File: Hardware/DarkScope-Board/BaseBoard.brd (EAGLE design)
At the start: 108 x 87.6 mm, 90 parts, among them IC1 7805DT, IC2 REG1117, IC3 7905, J1 DCJ0202, Q1 8MHz, T2 9014, U1 STM32F103CBT6, X1 TSW-102-07-G-S, X2 TSW-102-07-G-S, X3 MINI-USB-32005-301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

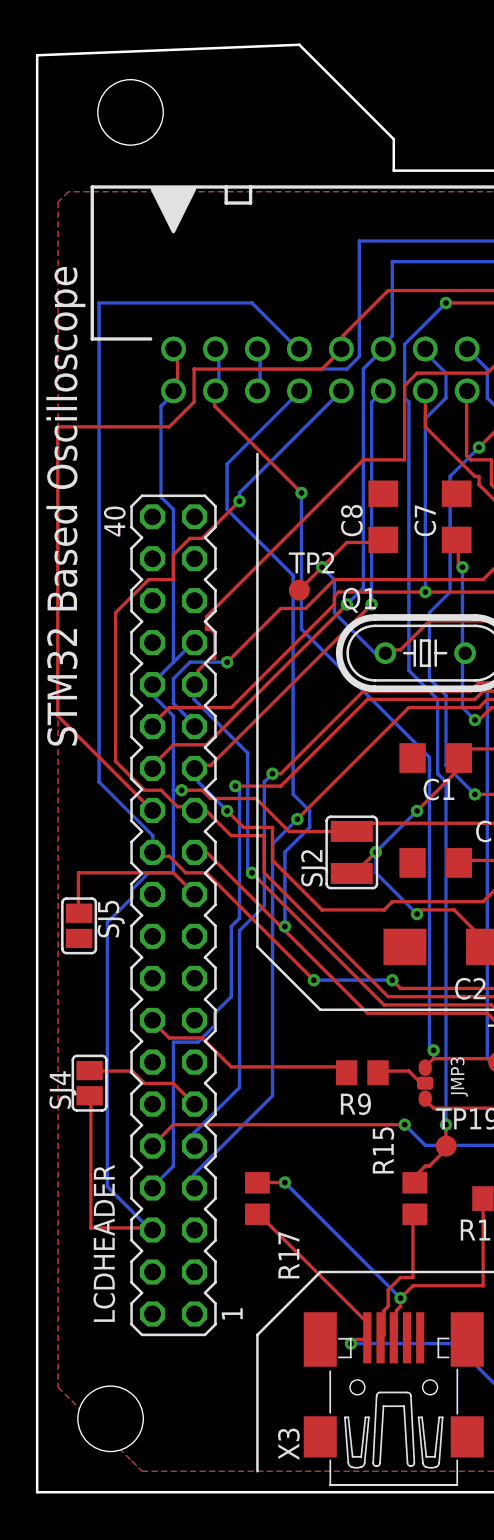
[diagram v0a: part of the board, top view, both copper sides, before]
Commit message: Updated Board Dimension and Added Gerbers
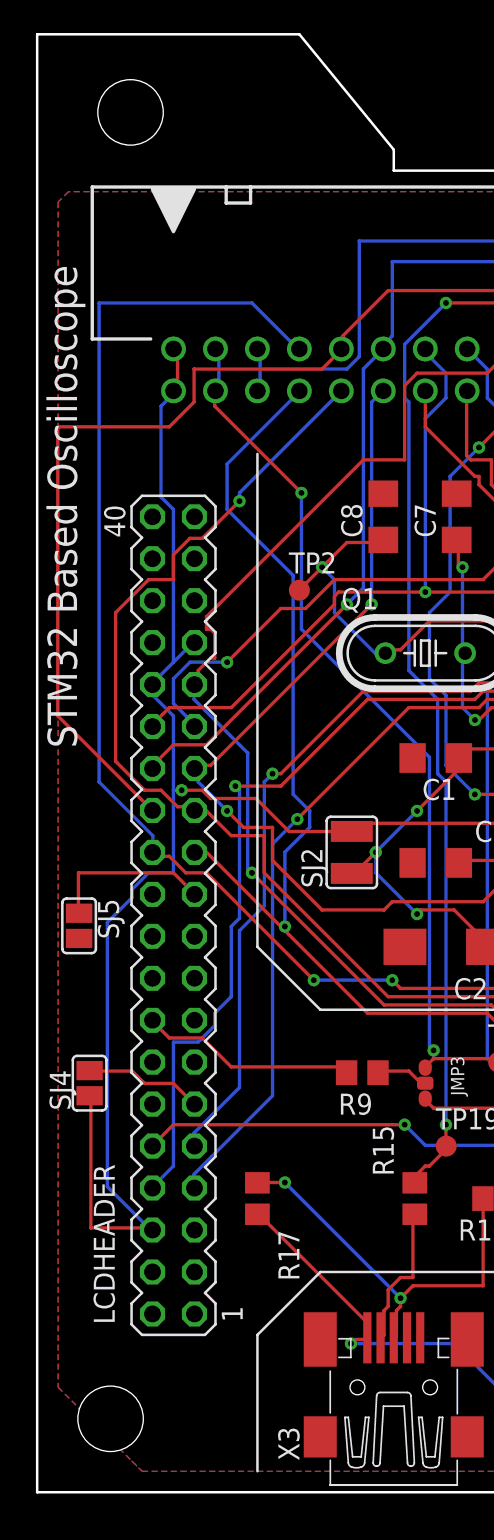
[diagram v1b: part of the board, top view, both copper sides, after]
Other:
- board size 108 x 87.6 mm -> 108 x 88.3 mm
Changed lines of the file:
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@@
 <drawing>
 <settings>
-<setting alwaysvectorfont="no"/>
+<setting alwaysvectorfont="yes"/>
 <setting verticaltext="up"/>
 </settings>
@@
 <wire x1="64.77" y1="3.81" x2="64.77" y2="1.27" width="0.1524" layer="25"/>
 <text x="77.47" y="76.835" size="1.778" layer="25">9V Max</text>
-<wire x1="0" y1="0" x2="0" y2="86.995" width="0.1524" layer="20"/>
-<wire x1="0" y1="86.995" x2="15.875" y2="87.63" width="0.1524" layer="20"/>
-<wire x1="15.875" y1="87.63" x2="21.59" y2="81.915" width="0.1524" layer="20"/>
-<wire x1="21.59" y1="81.915" x2="21.59" y2="80.01" width="0.1524" layer="20"/>
+<wire x1="0" y1="0" x2="0" y2="88.265" width="0.1524" layer="20"/>
+<wire x1="0" y1="88.265" x2="15.875" y2="88.265" width="0.1524" layer="20"/>
+<wire x1="15.875" y1="88.265" x2="21.59" y2="81.28" width="0.1524" layer="20"/>
+<wire x1="21.59" y1="81.28" x2="21.59" y2="80.01" width="0.1524" layer="20"/>
 <wire x1="21.59" y1="80.01" x2="78.74" y2="80.01" width="0.1524" layer="20"/>
 <wire x1="78.74" y1="80.01" x2="78.74" y2="82.55" width="0.1524" layer="20"/>

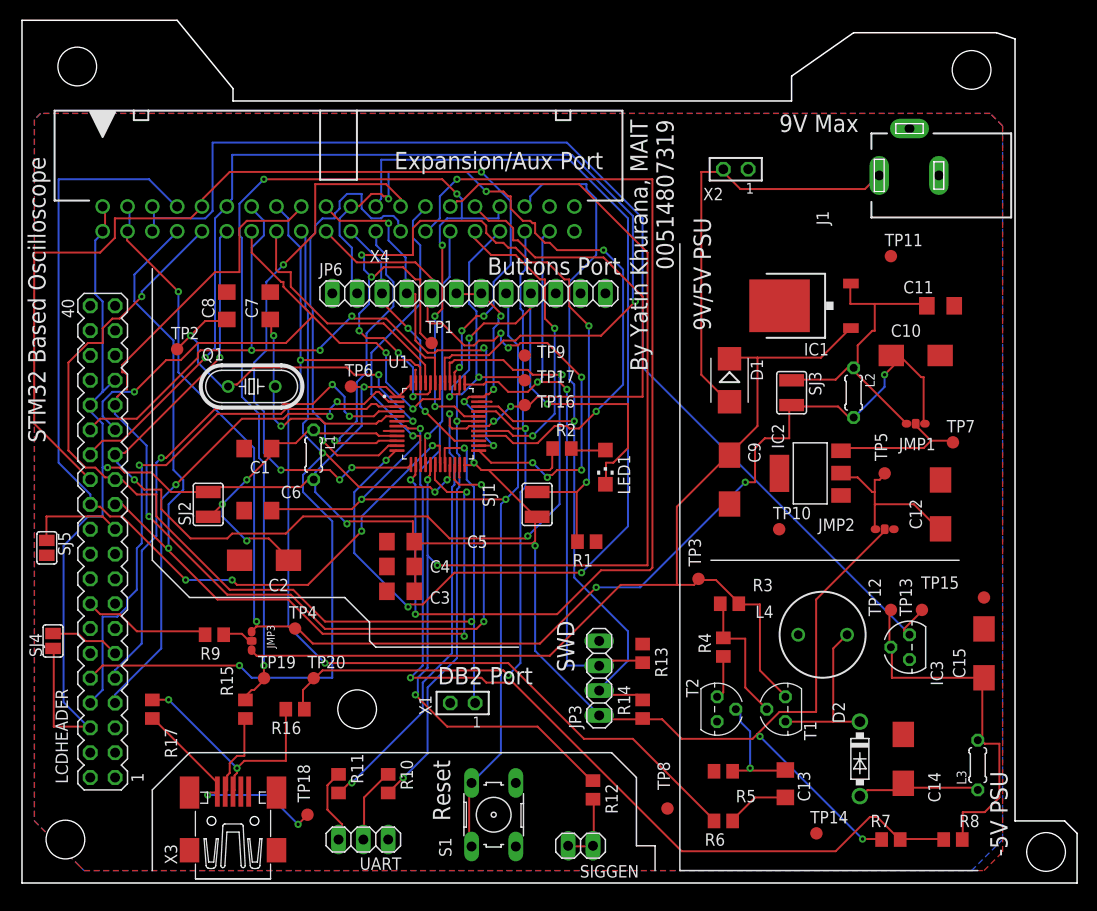
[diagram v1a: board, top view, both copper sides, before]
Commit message: Fixed BaseBoard Bugs
1. Ground Plane Not connected Properly
2. C14,C15 Reversed.
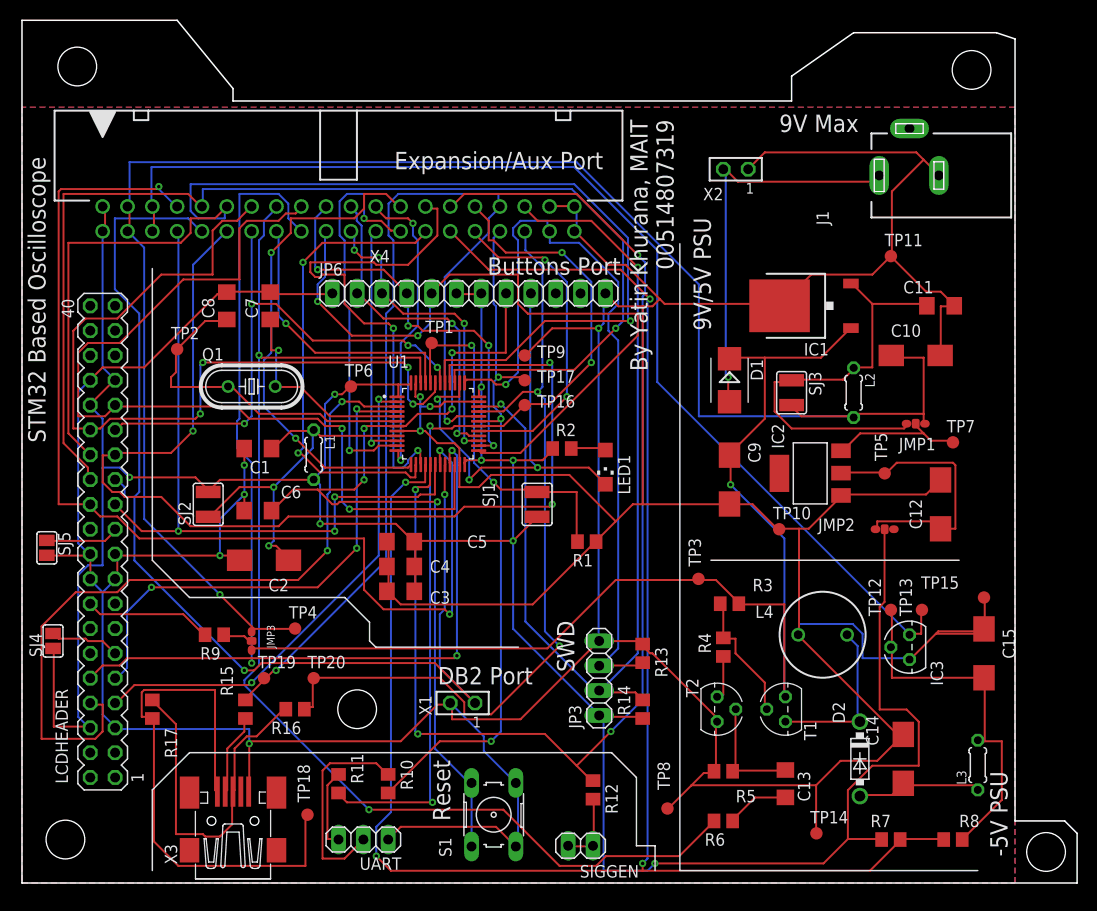
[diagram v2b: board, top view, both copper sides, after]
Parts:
- T1: value (none) -> 8550
- turned C14 to 270 degrees
- turned C15 to 270 degrees
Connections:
- net GND: now also C14.+, C15.+; no longer C14.-, C15.-
- net N$12: now also C14.-; no longer C14.+
- net N$13: now also C15.-; no longer C15.+
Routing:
- net GND: track 5.47 -> 584.9 mm, vias 0 -> 8
- net VSENSEL1: track 110.3 -> 31.2 mm, vias 3 -> 2
- net V-MON: track 116.8 -> 185.5 mm, vias 2 -> 4
- net ADCIN2: track 108.4 -> 48.0 mm, vias 3 -> 2
- net N$21: track 94.1 -> 37.4 mm, vias 7 -> 2
- net BTN1: track 76.4 -> 34.5 mm, vias 4 -> 2
- net N$26: track 23.3 -> 56.4 mm, vias 2 -> 0
- net +5V: track 144.4 -> 176.0 mm, vias 5 -> 1
- net LCD_NRD: track 91.5 -> 119.4 mm, vias 4 -> 3
- net DB0: track 98.7 -> 71.3 mm
- net DB7: track 60.7 -> 84.1 mm, vias 3 -> 4
- net +3V3: track 275.8 -> 299.0 mm, vias 10 -> 8
- net SWDIO: track 79.9 -> 100.2 mm, vias 1 -> 2
- net LCD_RS: track 56.6 -> 76.4 mm, vias 1 -> 2
- net ADCIN3: track 31.8 -> 51.6 mm, vias 1 -> 2
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
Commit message: Updated BaseBoard as per DFM Request
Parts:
- JMP1, JMP2, JMP3: value 0R-JUMPC -> 0R-JUMPA; device jump-0r-smd:C0R-JMP -> jump-0r-smd:A0R-JMP
- moved JMP3 1.27 mm to (23.5, 26.0)
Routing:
- net DB5: track 127.7 -> 72.8 mm
- net GND: track 584.9 -> 541.6 mm, vias 8 -> 6
- net +3V3: track 299.0 -> 340.0 mm, vias 8 -> 6
- net DB1: track 112.0 -> 76.0 mm
- net N$26: track 56.4 -> 22.4 mm, vias 0 -> 3
- net N$21: track 37.4 -> 69.4 mm
- net VGEN: track 127.2 -> 99.4 mm, vias 2 -> 4
- net TRIG: track 34.0 -> 57.9 mm, vias 2 -> 1
- net LCD_RS: track 76.4 -> 52.6 mm
- net BTN4: track 73.1 -> 50.9 mm, vias 2 -> 3
- net DB4: track 110.5 -> 88.3 mm, vias 3 -> 1
- net LCD_NCS: track 51.2 -> 71.3 mm, vias 2 -> 3
- net DB6: track 57.0 -> 76.9 mm, vias 4 -> 3
- net USBDM: track 98.5 -> 78.7 mm
- net TX1: track 92.6 -> 111.0 mm, vias 4 -> 2
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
